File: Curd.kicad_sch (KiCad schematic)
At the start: 67 parts, among them J1 Jack-DC, Q1 RQ3E120AT, Q10 PMV40UN2, Q11 RQ3E120AT, Q12 PMV40UN2, Q13 RQ3E120AT, Q14 PMV40UN2, Q15 RQ3E120AT, Q16 PMV40UN2, Q2 PMV40UN2, Q3 RQ3E120AT, Q4 PMV40UN2, Q5 RQ3E120AT, Q6 PMV40UN2, Q7 RQ3E120AT, Q8 PMV40UN2, Q9 RQ3E120AT, U1 OPA2192, U10 AP63203WU, U2 OPA2192, U3 DAC80508, U4 OPA2192, U5 OPA2192, U6 OPA2192, U7 OPA2192, U8 OPA2192, U9 OPA2192

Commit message: Added routing
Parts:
- removed C12: 22uF, Capacitor_SMD:C_0603_1608Metric, symbol Device:C_Small
- added R25, R26, R27, R28, R29, R30, R31, R32: ~, Resistor_SMD:R_0603_1608Metric, symbol Device:R_Small_US
- C11: value 22uF -> 10uF
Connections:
- net AVDD is gone; now on net V_IN: C1.1, C2.1, C3.1, C4.1, C5.1, C6.1, C7.1, C8.1, U1.8 (V+), U2.8 (V+), U4.8 (V+), U5.8 (V+), U6.8 (V+), U7.8 (V+), U8.8 (V+), U9.8 (V+)
- net DAC0: now also U1.5 (+), R25.2; no longer U1.6 (-), U3.2 (OUT0)
- net DAC1: now also U2.5 (+), R26.2; no longer U2.6 (-), U3.3 (OUT1)
- net DAC2: now also U4.5 (+), R27.2; no longer U3.4 (OUT2), U4.6 (-)
- net DAC3: now also U5.5 (+), R28.2; no longer U3.5 (OUT3), U5.6 (-)
- net DAC4: now also U6.5 (+), R29.2; no longer U3.8 (OUT4), U6.6 (-)
- net DAC5: now also U7.5 (+), R30.2; no longer U3.9 (OUT5), U7.6 (-)
- net DAC6: now also R31.2; no longer U3.10 (OUT6)
- net DAC7: now also U9.5 (+), R32.2; no longer U3.11 (OUT7), U9.6 (-)
- net at Q4.2, R6.1: now also U2.6 (-); no longer U2.5 (+)
- net at Q12.3, R16.2: now also U7.3 (+); no longer U7.2 (-)
- net at Q11.1, Q11.2 (S), Q11.3 (S)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: now also U7.2 (-); no longer U7.3 (+)
- net at Q8.2, R12.1: now also U5.6 (-); no longer U5.5 (+)
- net at Q16.2, R24.1: now also U9.6 (-); no longer U9.5 (+)
- net at Q16.3, R22.2: now also U9.3 (+); no longer U9.2 (-)
- net at Q1.1, Q1.2 (S), Q1.3 (S)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: now also U1.2 (-); no longer U1.3 (+)
- net at Q3.1, Q3.2 (S), Q3.3 (S)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: now also U2.2 (-); no longer U2.3 (+)
- net at Q5.1, Q5.2 (S), Q5.3 (S)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: now also U4.2 (-); no longer U4.3 (+)
- net at Q6.3, R7.2: now also U4.3 (+); no longer U4.2 (-)
- net at Q2.3, R1.2: now also U1.3 (+); no longer U1.2 (-)
- net at Q2.2, R3.1: now also U1.6 (-); no longer U1.5 (+)
- net at Q12.2, R18.1: now also U7.6 (-); no longer U7.5 (+)
- net at Q10.2, R15.1: now also U6.6 (-); no longer U6.5 (+)
- net at Q10.3, R13.2: now also U6.3 (+); no longer U6.2 (-)
- net at Q13.1, Q13.2 (S), Q13.3 (S)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: now also U8.2 (-); no longer U8.3 (+)
- net at Q7.1, Q7.2 (S), Q7.3 (S)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: now also U5.2 (-); no longer U5.3 (+)
- net at Q14.3, R19.2: now also U8.3 (+); no longer U8.2 (-)
- net at Q8.3, R10.2: now also U5.3 (+); no longer U5.2 (-)
- net at Q6.2, R9.1: now also U4.6 (-); no longer U4.5 (+)
- net at Q9.1, Q9.2 (S), Q9.3 (S)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: now also U6.2 (-); no longer U6.3 (+)
- net at Q4.3, R4.2: now also U2.3 (+); no longer U2.2 (-)
- net at Q15.1, Q15.2 (S), Q15.3 (S)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: now also U9.2 (-); no longer U9.3 (+)
- new net: R31.1, U3.10 (OUT6)
- new net: R32.1, U3.11 (OUT7)
- new net: R30.1, U3.9 (OUT5)
- new net: R27.1, U3.4 (OUT2)
- new net: R29.1, U3.8 (OUT4)
- new net: R25.1, U3.2 (OUT0)
- new net: R26.1, U3.3 (OUT1)
- new net: R28.1, U3.5 (OUT3)

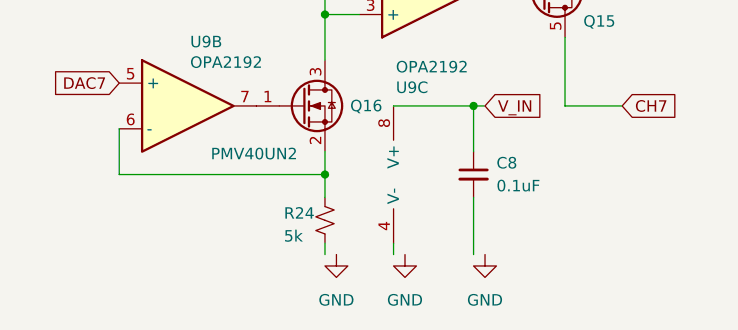
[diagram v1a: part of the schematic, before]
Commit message: Updated routing
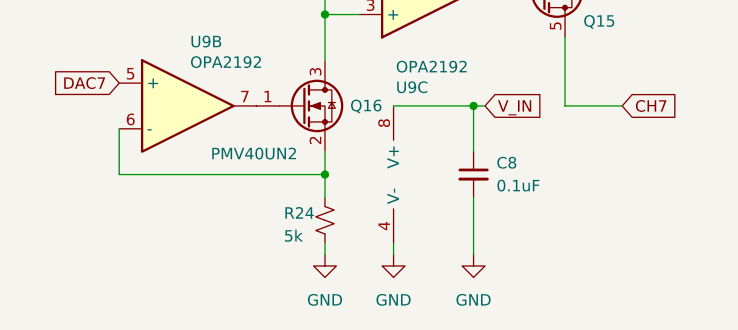
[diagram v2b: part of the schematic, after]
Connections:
- net GND: now also C8.2, R24.2, U9.4 (V-)
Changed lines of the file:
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@@
 	(symbol
 		(lib_id "power:GND")
-		(at 377.19 237.49 0)
+		(at 375.92 237.49 0)
 		(unit 1)
 		(exclude_from_sim no)
@@
 		(fields_autoplaced yes)
 		(property "Reference" "#PWR059"
-			(at 377.19 243.84 0)
+			(at 375.92 243.84 0)
 			(effects
 				(font
@@
 		)
 		(property "Value" "GND"
-			(at 377.19 242.57 0)
+			(at 375.92 242.57 0)
 			(effects
 				(font
@@
 		)
 		(property "Footprint" ""
-			(at 377.19 237.49 0)
+			(at 375.92 237.49 0)
 			(effects
 				(font
@@
 		)
 		(property "Datasheet" ""
-			(at 377.19 237.49 0)
+			(at 375.92 237.49 0)
 			(effects
 				(font
@@
 		)
 		(property "Description" "Power symbol creates a global label with name \"GND\" , ground"
-			(at 377.19 237.49 0)
+			(at 375.92 237.49 0)
 			(effects
 				(font
@@
 	(symbol
 		(lib_id "power:GND")
-		(at 360.68 237.49 0)
+		(at 359.41 237.49 0)
 		(unit 1)
 		(exclude_from_sim no)
@@
 		(fields_autoplaced yes)
 		(property "Reference" "#PWR057"
-			(at 360.68 243.84 0)
+			(at 359.41 243.84 0)
 			(effects
 				(font
@@
 		)
 		(property "Value" "GND"
-			(at 360.68 242.57 0)
+			(at 359.41 242.57 0)
 			(effects
 				(font
@@
 		)
 		(property "Footprint" ""
-			(at 360.68 237.49 0)
+			(at 359.41 237.49 0)
 			(effects
 				(font
@@
 		)
 		(property "Datasheet" ""
-			(at 360.68 237.49 0)
+			(at 359.41 237.49 0)
 			(effects
 				(font
@@
 		)
 		(property "Description" "Power symbol creates a global label with name \"GND\" , ground"
-			(at 360.68 237.49 0)
+			(at 359.41 237.49 0)
 			(effects
 				(font
@@
 	(symbol
 		(lib_id "power:GND")
-		(at 368.3 237.49 0)
+		(at 367.03 237.49 0)
 		(unit 1)
 		(exclude_from_sim no)
@@
 		(fields_autoplaced yes)
 		(property "Reference" "#PWR058"
-			(at 368.3 243.84 0)
+			(at 367.03 243.84 0)
 			(effects
 				(font
@@
 		)
 		(property "Value" "GND"
-			(at 368.3 242.57 0)
+			(at 367.03 242.57 0)
 			(effects
 				(font
@@
 		)
 		(property "Footprint" ""
-			(at 368.3 237.49 0)
+			(at 367.03 237.49 0)
 			(effects
 				(font
@@
 		)
 		(property "Datasheet" ""
-			(at 368.3 237.49 0)
+			(at 367.03 237.49 0)
 			(effects
 				(font
@@
 		)
 		(property "Description" "Power symbol creates a global label with name \"GND\" , ground"
-			(at 368.3 237.49 0)
+			(at 367.03 237.49 0)
 			(effects
 				(font
